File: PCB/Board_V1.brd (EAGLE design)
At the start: 19.4 x 48.6 mm, 8 parts, among them X2 USB-B-H

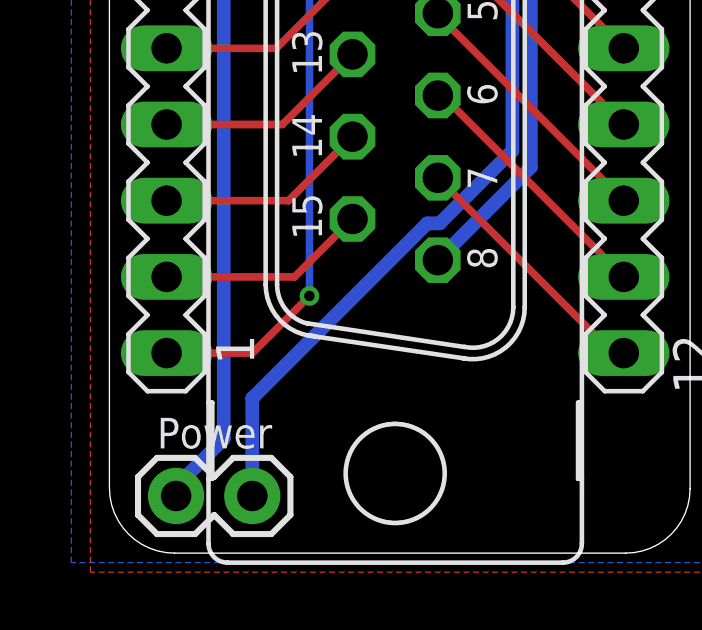
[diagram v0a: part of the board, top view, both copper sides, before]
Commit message: Add files via upload
Minor changes on GND layer
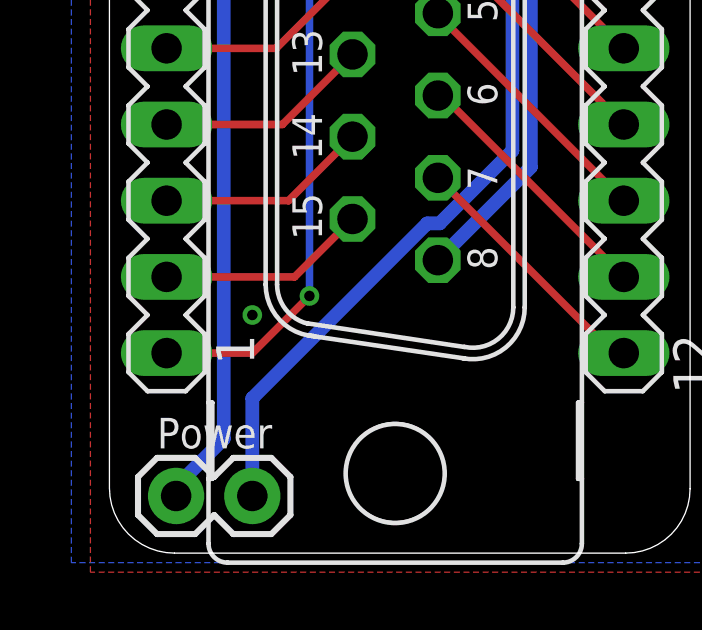
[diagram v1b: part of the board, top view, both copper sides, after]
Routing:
- net GND: vias 0 -> 1
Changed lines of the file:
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@@
 <wire x1="3.81" y1="8.5725" x2="3.81" y2="33.02" width="0.4572" layer="16"/>
 <wire x1="3.81" y1="33.02" x2="2.54" y2="34.29" width="0.4572" layer="16"/>
-<wire x1="3.81" y1="33.02" x2="1.905" y2="31.75" width="0" layer="19" extent="16-16"/>
+<via x="4.7625" y="12.7" extent="1-16" drill="0.35"/>
 </signal>
 <signal name="DWN">
